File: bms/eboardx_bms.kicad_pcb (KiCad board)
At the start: 2 copper layers, 56 x 60 mm, 173 parts, among them J1 Balance connector, P1 BAT+, P2 P+, P3 P-, P4 BAT-, Q1 BFS20, Q10 UMW 30N06, Q11 UMW 30N06, Q12 UMW 30N06, Q13 UMW 30N06, Q14 MMBT5401, Q15 MMBT5401, Q16 MMBT5401, Q17 MMBT5401, Q18 MMBT5401, Q19 MMBT5401, Q2 BFS20, Q20 MMBT5401, Q21 MMBT5401, Q22 MMBT5401, Q23 MMBT5401, Q24 MMBT5401, Q25 MMBT5401, Q26 MMBT5401, Q27 MMBT5401, Q28 MMBT5401, Q29 MMBT5401, Q3 BFS20, Q30 MMBT5401, Q31 MMBT5401, Q32 MMBT5401, Q33 MMBT5401, Q34 A2SHB, Q35 A2SHB, Q36 A2SHB, Q37 A2SHB, Q38 A2SHB, Q39 A2SHB, Q4 UMW 30N06, Q40 A2SHB, Q41 A2SHB, Q42 A2SHB, Q43 A2SHB, Q44 A2SHB, Q5 UMW 30N06, Q6 UMW 30N06, Q7 UMW 30N06, Q8 UMW 30N06, Q9 UMW 30N06, U1 DW01B, U10 DW01B, U11 HY2213-BB3A, U12 HY2213-BB3A, U13 HY2213-BB3A, U14 HY2213-BB3A, U15 HY2213-BB3A, U16 HY2213-BB3A, U17 HY2213-BB3A, U18 HY2213-BB3A, U19 HY2213-BB3A, U2 DW01B, U20 HY2213-BB3A, U3 DW01B, U4 DW01B, U5 DW01B, U6 DW01B, U7 DW01B, U8 DW01B, U9 DW01B

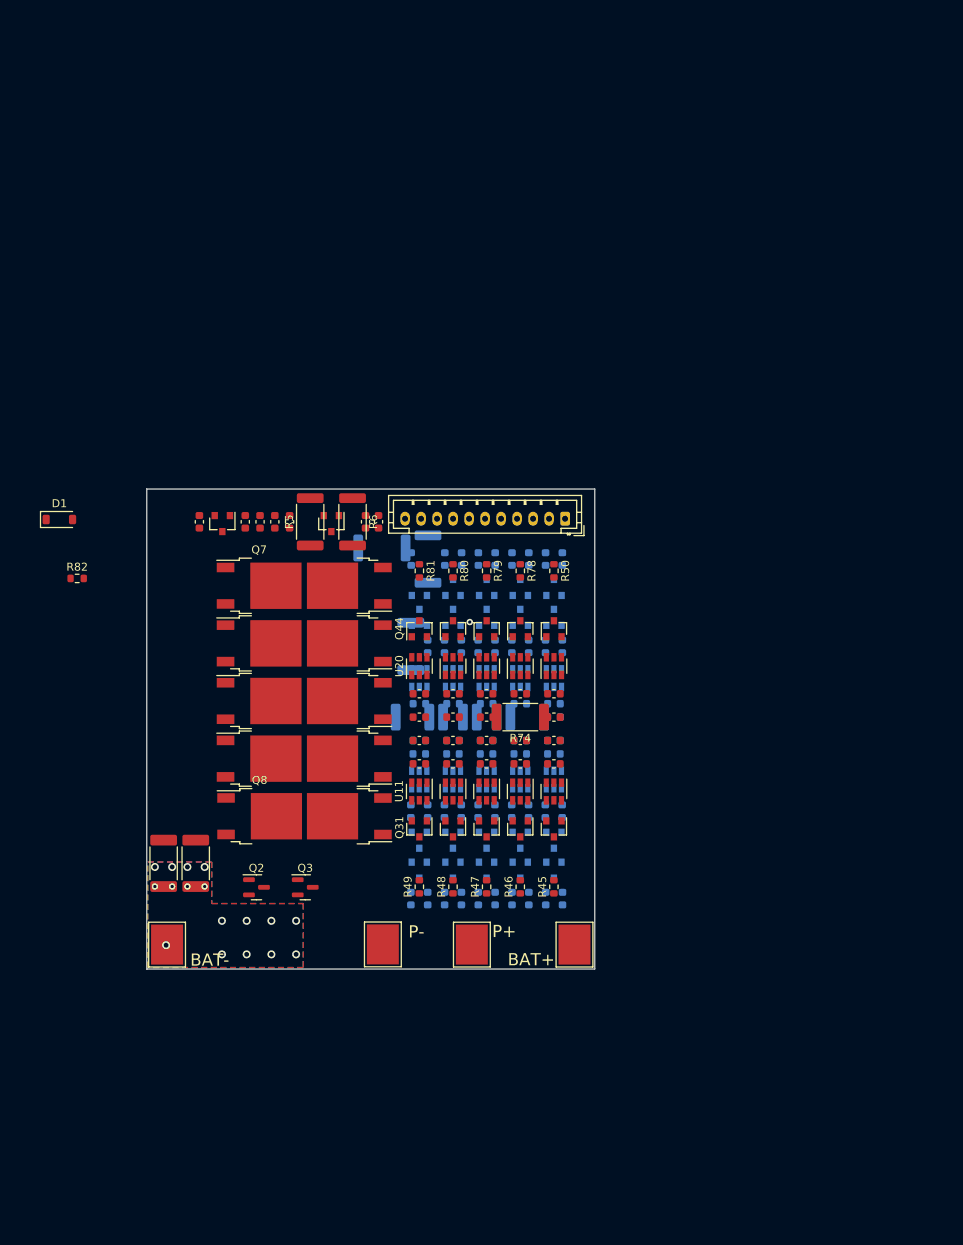
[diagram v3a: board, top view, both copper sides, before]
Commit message: bms change to 13s1p
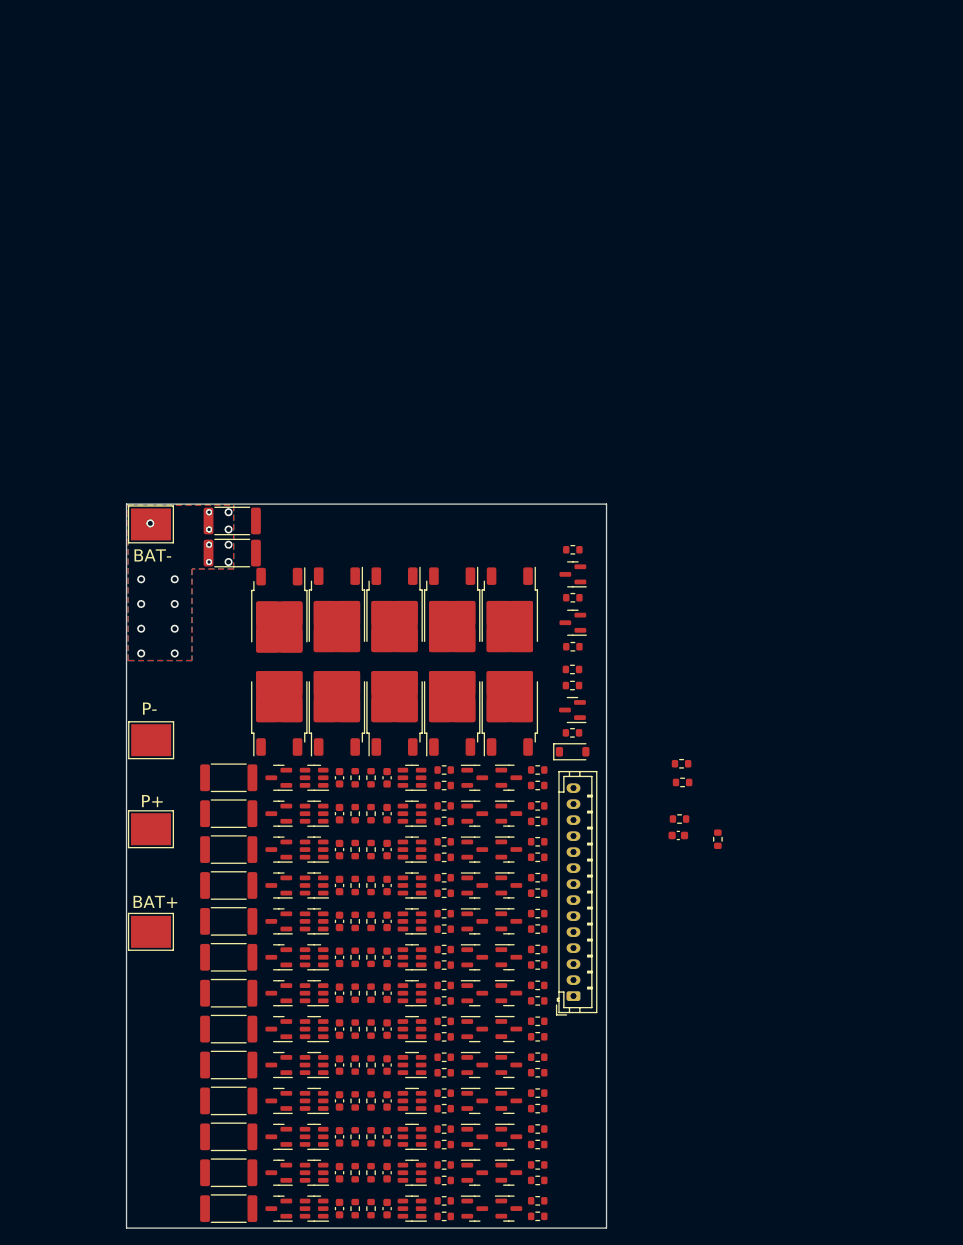
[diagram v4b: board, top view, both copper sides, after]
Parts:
- removed the R4 at (69.6, 46.0)
- removed the R5 at (83.4, 46.0)
- removed the R6 at (88.7, 46.0)
- added C11: 0.1u, Capacitor_SMD:C_0603_1608Metric, F.Cu at (93.0, 122.9)
- added C12: 0.1u, Capacitor_SMD:C_0603_1608Metric, F.Cu at (93.0, 127.4)
- added C13: 0.1u, Capacitor_SMD:C_0603_1608Metric, F.Cu at (93.0, 131.9)
- added C24: 0.1u, Capacitor_SMD:C_0603_1608Metric, F.Cu at (87.1, 122.9)
- added C25: 0.1u, Capacitor_SMD:C_0603_1608Metric, F.Cu at (87.1, 127.4)
- added C26: 0.1u, Capacitor_SMD:C_0603_1608Metric, F.Cu at (87.1, 131.9)
- added Q21: A2SHB, Package_TO_SOT_SMD:SOT-23, F.Cu at (79.5, 122.9)
- added Q22: A2SHB, Package_TO_SOT_SMD:SOT-23, F.Cu at (79.5, 127.4)
- added Q23: A2SHB, Package_TO_SOT_SMD:SOT-23, F.Cu at (79.5, 131.9)
- added Q45: MMBT5401, Package_TO_SOT_SMD:SOT-23, F.Cu at (108.3, 122.9)
- added Q46: MMBT5401, Package_TO_SOT_SMD:SOT-23, F.Cu at (104.0, 127.4)
- added Q47: MMBT5401, Package_TO_SOT_SMD:SOT-23, F.Cu at (108.3, 127.4)
- added Q48: MMBT5401, Package_TO_SOT_SMD:SOT-23, F.Cu at (104.0, 131.9)
- added Q49: MMBT5401, Package_TO_SOT_SMD:SOT-23, F.Cu at (108.3, 131.9)
- added R101: 1k, Resistor_SMD:R_0603_1608Metric, F.Cu at (129.6, 83.2)
- added R102: R005, Resistor_SMD:R_2512_6332Metric, F.Cu at (73.7, 49.9)
- added R103: R005, Resistor_SMD:R_2512_6332Metric, F.Cu at (73.7, 45.9)
- added R11: 100, Resistor_SMD:R_0603_1608Metric, F.Cu at (91.0, 122.9)
- added R12: 100, Resistor_SMD:R_0603_1608Metric, F.Cu at (91.0, 127.4)
- added R13: 100, Resistor_SMD:R_0603_1608Metric, F.Cu at (91.0, 131.9)
- added R24: 100, Resistor_SMD:R_0603_1608Metric, F.Cu at (89.0, 122.9)
- added R25: 100, Resistor_SMD:R_0603_1608Metric, F.Cu at (89.0, 127.4)
- added R26: 100, Resistor_SMD:R_0603_1608Metric, F.Cu at (89.0, 131.9)
- added R37: 68, Resistor_SMD:R_2512_6332Metric, F.Cu at (73.2, 122.9)
- added R38: 68, Resistor_SMD:R_2512_6332Metric, F.Cu at (73.2, 127.4)
- added R39: 68, Resistor_SMD:R_2512_6332Metric, F.Cu at (73.2, 131.9)
- added R60: 510k, Resistor_SMD:R_0603_1608Metric, F.Cu at (100.2, 121.9)
- added R61: 510k, Resistor_SMD:R_0603_1608Metric, F.Cu at (100.2, 123.9)
- added R62: 510k, Resistor_SMD:R_0603_1608Metric, F.Cu at (100.2, 126.4)
- added R63: 510k, Resistor_SMD:R_0603_1608Metric, F.Cu at (100.2, 128.3)
- added R64: 510k, Resistor_SMD:R_0603_1608Metric, F.Cu at (100.2, 130.9)
- added R65: 510k, Resistor_SMD:R_0603_1608Metric, F.Cu at (100.2, 132.8)
- added R86: 1M, Resistor_SMD:R_0603_1608Metric, F.Cu at (111.9, 121.9)
- added R87: 1M, Resistor_SMD:R_0603_1608Metric, F.Cu at (111.9, 123.8)
- added R88: 1M, Resistor_SMD:R_0603_1608Metric, F.Cu at (111.9, 126.4)
- added R89: 1M, Resistor_SMD:R_0603_1608Metric, F.Cu at (111.9, 128.3)
- added R90: 1M, Resistor_SMD:R_0603_1608Metric, F.Cu at (111.9, 130.9)
- added R91: 1M, Resistor_SMD:R_0603_1608Metric, F.Cu at (111.9, 132.8)
- added U11: DW01B, Package_TO_SOT_SMD:SOT-23-6, F.Cu at (96.2, 122.9)
- added U12: DW01B, Package_TO_SOT_SMD:SOT-23-6, F.Cu at (96.2, 127.4)
- added U13: DW01B, Package_TO_SOT_SMD:SOT-23-6, F.Cu at (96.2, 131.9)
- added U24: HY2213-BB3A, Package_TO_SOT_SMD:SOT-23-6, F.Cu at (83.9, 122.9)
- added U25: HY2213-BB3A, Package_TO_SOT_SMD:SOT-23-6, F.Cu at (83.9, 127.4)
- added U26: HY2213-BB3A, Package_TO_SOT_SMD:SOT-23-6, F.Cu at (83.9, 131.9)
- C1: renamed from C2; moved to F.Cu
- C16: renamed from C14; moved to F.Cu
- C17: renamed from C15; moved to F.Cu
- C18: renamed from C16; moved to F.Cu
- C19: renamed from C17; moved to F.Cu
- C2: renamed from C3; moved to F.Cu
- C3: renamed from C4; moved to F.Cu
- C4: renamed from C5; moved to F.Cu
- C5: renamed from C6; moved to F.Cu
- C6: renamed from C7; moved to F.Cu
- J1: footprint Connector_JST:JST_PH_B11B-PH-K_1x11_P2.00mm_Vertical -> Connector_JST:JST_PH_B14B-PH-K_1x14_P2.00mm_Vertical
- Q11: renamed from Q34; moved to F.Cu
- Q12: renamed from Q35; moved to F.Cu
- Q13: renamed from Q36; moved to F.Cu
- Q14: renamed from Q37; moved to F.Cu
- Q15: renamed from Q38; moved to F.Cu
- Q16: renamed from Q39; moved to F.Cu
- Q17: renamed from Q40; moved to F.Cu
- Q25: renamed from Q15; moved to F.Cu
- Q26: renamed from Q16; moved to F.Cu
- Q27: renamed from Q17; moved to F.Cu
- Q28: renamed from Q18; moved to F.Cu
- Q29: renamed from Q19; moved to F.Cu
- Q30: renamed from Q20; moved to F.Cu
- Q31: renamed from Q21; moved to F.Cu
- Q32: renamed from Q22; moved to F.Cu
- Q33: renamed from Q23; moved to F.Cu
- Q34: renamed from Q24; moved to F.Cu
- Q35: renamed from Q25; moved to F.Cu
- Q36: renamed from Q26; moved to F.Cu
- Q43: renamed from Q33; moved to F.Cu
- Q44: value A2SHB -> MMBT5401
- R10: renamed from R14; moved to F.Cu
- R14: renamed from R55; moved to F.Cu
- R15: renamed from R56; moved to F.Cu
- R16: renamed from R57; moved to F.Cu
- R17: renamed from R58; moved to F.Cu
- R18: renamed from R59; moved to F.Cu
- R19: renamed from R60; moved to F.Cu
- R20: renamed from R61; moved to F.Cu
- R21: renamed from R62; moved to F.Cu
- R22: renamed from R63; moved to F.Cu
- R23: renamed from R64; moved to F.Cu
- R27: renamed from R65; moved to F.Cu
- R28: renamed from R66; moved to F.Cu
- R29: renamed from R67; moved to F.Cu
- R31: renamed from R69; moved to F.Cu
- R32: renamed from R70; moved to F.Cu
- R33: renamed from R71; moved to F.Cu
- R34: renamed from R72; moved to F.Cu
- R40: renamed from R35; moved to F.Cu
- R41: renamed from R36; moved to F.Cu
- R42: renamed from R37; moved to F.Cu
- R43: renamed from R38; moved to F.Cu
- R5: renamed from R9; moved to F.Cu
- R56: renamed from R51; moved to F.Cu
- R57: renamed from R52; moved to F.Cu
- R58: renamed from R53; moved to F.Cu
- R59: renamed from R54; moved to F.Cu
- R6: renamed from R10; moved to F.Cu
- R66: renamed from R15; moved to F.Cu
- R67: renamed from R16; moved to F.Cu
- R68: renamed from R17; moved to F.Cu
- R69: renamed from R18; moved to F.Cu
- R7: renamed from R11; moved to F.Cu
- R70: renamed from R19; moved to F.Cu
- R71: renamed from R20; moved to F.Cu
- R72: renamed from R21; moved to F.Cu
- R73: renamed from R22; moved to F.Cu
- R74: renamed from R23; moved to F.Cu
- R75: renamed from R24; moved to F.Cu
- R76: renamed from R25; moved to F.Cu
- R77: renamed from R26; moved to F.Cu
- R78: renamed from R27; moved to F.Cu
- R79: renamed from R28; moved to F.Cu
- R8: renamed from R12; moved to F.Cu
- R80: renamed from R29; moved to F.Cu
- R81: renamed from R30; moved to F.Cu
- R82: renamed from R31; moved to F.Cu
- R83: renamed from R32; moved to F.Cu
- R84: renamed from R33; moved to F.Cu
- R85: renamed from R34; moved to F.Cu
- R9: renamed from R13; moved to F.Cu
- U1, U2, U3, U4, U5, U6: moved to F.Cu
- U16: renamed from U13; moved to F.Cu
- U17: renamed from U14; moved to F.Cu
- U18: renamed from U15; moved to F.Cu
- U19: renamed from U16; moved to F.Cu
- moved D1 70.4 mm to (116.2, 74.8)
- moved R59 69.5 mm to (100.2, 119.4), turned to 0 degrees
- moved C27 66.8 mm to (129.4, 85.2), turned to 0 degrees
- moved R17 65.6 mm to (89.0, 113.9), turned to 90 degrees
- moved R83 64.3 mm to (111.9, 114.9), turned to 0 degrees
- moved Q44 63.9 mm to (104.0, 122.9), turned to 0 degrees
- moved Q20 62.9 mm to (79.5, 118.4), turned to 180 degrees
- moved R56 62.9 mm to (100.2, 112.9), turned to 0 degrees
- moved R93 62.1 mm to (116.3, 49.5)
- moved Q43 60.5 mm to (108.3, 118.4), turned to 0 degrees
- moved Q19 60.4 mm to (79.5, 113.9), turned to 180 degrees
- moved R36 60.2 mm to (73.2, 118.4), turned to 0 degrees
- moved R55 59.8 mm to (100.2, 110.4), turned to 180 degrees
- moved Q42 59.8 mm to (104.0, 118.4), turned to 0 degrees
- moved R18 59.8 mm to (89.0, 109.4), turned to 90 degrees
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- renumbered C11 to C10, C12 to C14, C13 to C15, C18 to C20, C19 to C21, C20 to C22, C21 to C23, C1 to C27, C8 to C7, C9 to C8, C10 to C9, Q4 to Q1, Q13 to Q10, Q41 to Q18, Q42 to Q19, Q5 to Q2, Q43 to Q20, Q14 to Q24, Q6 to Q3, Q27 to Q37, Q28 to Q38, Q29 to Q39, Q7 to Q4, Q30 to Q40, Q31 to Q41, Q32 to Q42, Q8 to Q5, Q1 to Q50, Q2 to Q51, Q3 to Q52, Q9 to Q6, Q10 to Q7, Q11 to Q8, Q12 to Q9, R2 to R1, R81 to R100, R3 to R2, R7 to R3, R68 to R30, R73 to R35, R74 to R36, R8 to R4, R39 to R44, R40 to R45, R41 to R46, R42 to R47, R43 to R48, R44 to R49, R45 to R50, R46 to R51, R47 to R52, R48 to R53, R49 to R54, R50 to R55, R75 to R92, R82 to R93, R1 to R94, R76 to R95, R77 to R96, R78 to R97, R79 to R98, R80 to R99, U11 to U14, U12 to U15, U17 to U20, U18 to U21, U19 to U22, U20 to U23
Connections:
- net /Balance charge and over current detection/OC1 renamed /Protection for BAT1-10/OC1
- net /Balance charge and over current detection/OC2 renamed /Protection for BAT1-10/OC2
- net /Balance charge and over current detection/OC3 renamed /Protection for BAT1-10/OC3
- net /Balance charge and over current detection/OC4 renamed /Protection for BAT1-10/OC4
- net /Balance charge and over current detection/OC5 renamed /Protection for BAT1-10/OC5
- net /Balance charge and over current detection/OC6 renamed /Protection for BAT1-10/OC6
- net /Balance charge and over current detection/OC7 renamed /Protection for BAT1-10/OC7
- net /Balance charge and over current detection/OC8 renamed /Protection for BAT1-10/OC8
- net /Balance charge and over current detection/OC9 renamed /Protection for BAT1-10/OC9
- net /Balance charge and over current detection/OD1 renamed /Protection for BAT1-10/OD1
- net /Balance charge and over current detection/OD2 renamed /Protection for BAT1-10/OD2
- net /Balance charge and over current detection/OD3 renamed /Protection for BAT1-10/OD3
- net /Balance charge and over current detection/OD4 renamed /Protection for BAT1-10/OD4
- net /Balance charge and over current detection/OD5 renamed /Protection for BAT1-10/OD5
- net /Balance charge and over current detection/OD6 renamed /Protection for BAT1-10/OD6
- net /Balance charge and over current detection/OD7 renamed /Protection for BAT1-10/OD7
- net /Balance charge and over current detection/OD8 renamed /Protection for BAT1-10/OD8
- net /Balance charge and over current detection/OD9 renamed /Protection for BAT1-10/OD9
- C10 pad 2: /BAT- -> Net-(Q20-S)
- C23 pad 2: /BAT- -> Net-(Q20-S)
- J1 pad 11: /BAT- -> /BAT11
- Q20 pad 2: /BAT- -> Net-(Q20-S)
- Q44 pad 2: /BAT- -> /BAT11
- Q44 pad 3: Net-(Q44-Pad3) -> /Protection for BAT1-10/OD10
- R84 pad 1: /ChargeControl -> /Protection for BAT1-10/OC10
- R85 pad 1: /DischargeControl -> /Protection for BAT1-10/OD10
- R96 pad 2: /BAT7 -> /BAT10
- R97 pad 2: /BAT7 -> /BAT10
- U10 pad 2: Net-(U10-CS) -> Net-(Q20-S)
- U10 pad 6: /BAT- -> Net-(Q20-S)
- U23 pad 3: /BAT- -> Net-(Q20-S)
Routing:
- net /BAT9: vias 3 -> 0
- net /BAT4: vias 2 -> 0
- net /BAT-: vias 13 -> 17
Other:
- board size 56 x 60 mm -> 60 x 90.5 mm

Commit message: bms pcb
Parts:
- moved J1 20.0 mm to (117.4, 85.3), turned to -90 degrees
- moved Q10 3.92 mm to (108.3, 65.2)
- moved Q6 3.92 mm to (79.5, 65.2)
- moved Q7 3.92 mm to (86.7, 65.2)
- moved Q8 3.92 mm to (93.9, 65.2)
- moved Q9 3.92 mm to (101.1, 65.2)
- moved Q5 2.88 mm to (79.5, 55.0)
- moved Q1 2.82 mm to (86.7, 55.0)
- moved Q2 2.82 mm to (93.9, 55.0)
- moved Q3 2.82 mm to (101.1, 55.0)
- moved Q4 2.82 mm to (108.3, 55.0)
- moved Q50 2.48 mm to (116.1, 50.1)
- moved R93 2.48 mm to (116.1, 47.0)
- moved D1 2.48 mm to (116.1, 72.3)
- moved Q51 2.48 mm to (116.1, 56.1)
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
